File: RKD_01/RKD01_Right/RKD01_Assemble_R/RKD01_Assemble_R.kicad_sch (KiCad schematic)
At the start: 95 parts, among them J2 TRRS, M1 Mark, M2 Mark, M3 Mark, M4 Mark, M5 Mark, M6 Mark, P1 pointing, SW51 SW_Push, SW52 SW_Push, SW53 SW_Push, SW54 SW_Push, SW55 SW_Push, SW56 SW_Push, SW57 SW_Push, SW58 SW_Push, SW59 SW_Push, SW60 SW_Push, SW61 SW_Push, SW62 SW_Push, SW63 SW_Push, SW64 SW_Push, SW65 SW_Push, SW66 SW_Push, SW67 SW_Push, SW68 SW_Push, SW69 SW_Push, SW70 SW_Push, SW71 SW_Push, SW72 SW_Push, SW73 SW_Push, SW74 SW_Push, SW75 SW_Push, SW76 SW_Push, SW77 SW_Push, SW78 SW_Push, SW79 SW_Push, SW80 SW_Push, SW81 SW_Push, SW82 SW_Push, SW83 SW_Push, SW84 SW_Push, SW85 SW_Push, SW86 SW_Push, SW87 SW_Push, SW88 SW_Push, SW89 SW_Push, SW90 SW_Push, SW91 SW_Push, SW92 SW_Push, SW93 SW_Push, U2 ProMicro

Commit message: v1.5
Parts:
- added D75: D, kbd_Parts:Diode_TH_SMD, symbol Device:D
- added M7, M8: Mark, kbd_Hole:m2_Spacer_Hole_hex, symbol BrownSugar_KBD:Mark
- added SW75: SW_Push, kbd_SW:Choc_Hotswap_1u, symbol Switch:SW_Push
- renumbered D75 to D76, D76 to D77, D77 to D78, D78 to D79, D79 to D80, D80 to D81, D81 to D82, D82 to D83, D83 to D84, D84 to D85, D85 to D86, D86 to D87, D87 to D88, D88 to D89, D89 to D90, D90 to D91, D91 to D92, D92 to D94, D93 to D95, SW75 to SW76, SW76 to SW77, SW77 to SW78, SW78 to SW79, SW79 to SW80, SW80 to SW81, SW81 to SW82, SW82 to SW83, SW83 to SW84, SW84 to SW85, SW85 to SW86, SW86 to SW87, SW87 to SW88, SW88 to SW89, SW89 to SW90, SW90 to SW91, SW91 to SW92, SW92 to SW94, SW93 to SW95
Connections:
- net Col4: now also SW75.2
- net Row4: now also D75.1 (K)
- new net: D75.2 (A), SW75.1

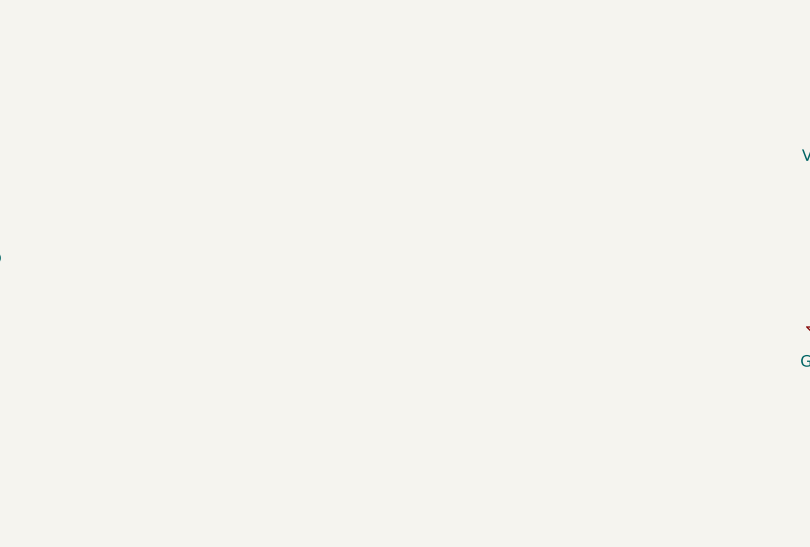
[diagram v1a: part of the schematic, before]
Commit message: OLEDを追加
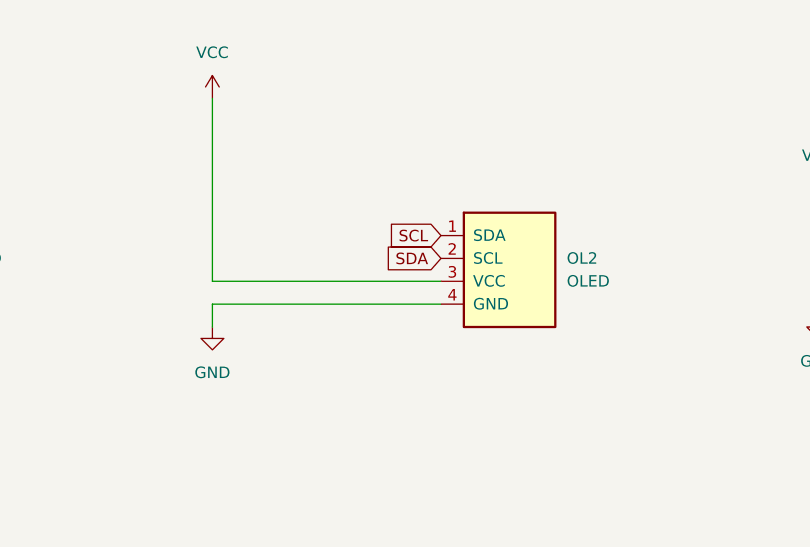
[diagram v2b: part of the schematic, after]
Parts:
- added OL2: OLED, BrownSugar_KBD:OLED_center_module, symbol BrownSugar_KBD:OLED
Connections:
- net GND: now also OL2.4 (GND)
- net SCL: now also OL2.1 (SDA)
- net SDA: now also OL2.2 (SCL)
- net VCC: now also OL2.3 (VCC)

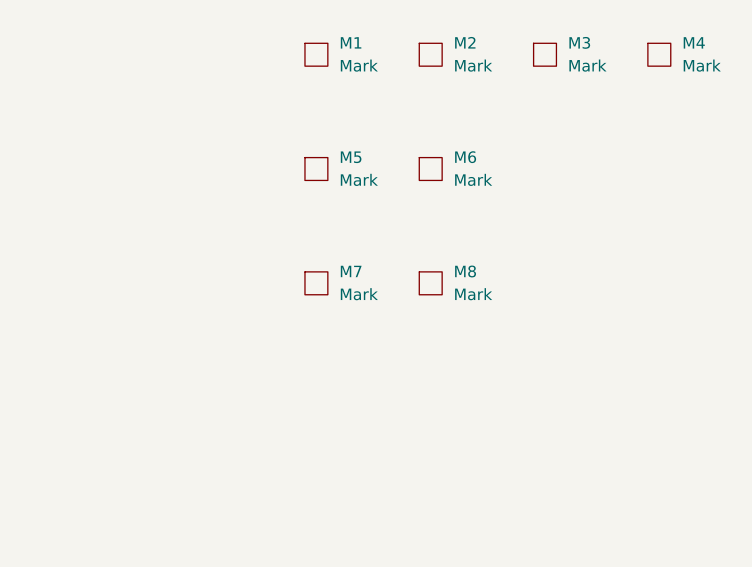
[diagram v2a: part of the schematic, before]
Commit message: スイッチフットプリントをChocV2に修正
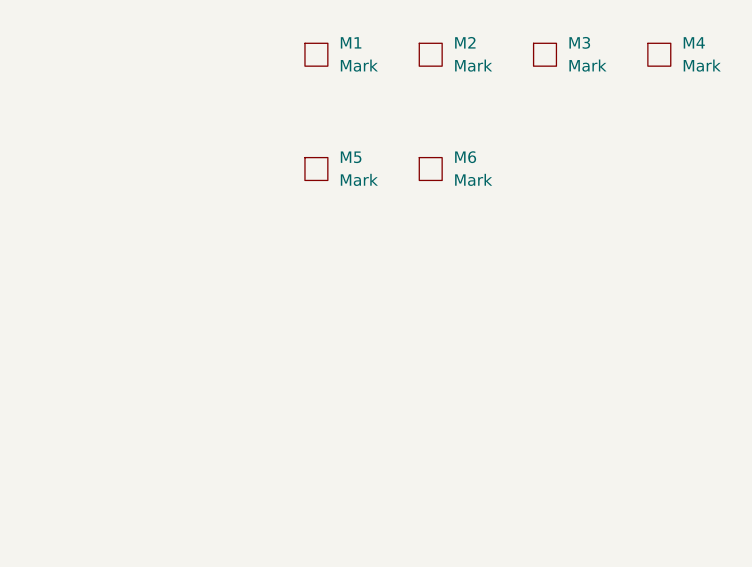
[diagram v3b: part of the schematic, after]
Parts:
- removed M7, M8: Mark, kbd_Hole:m2_Spacer_Hole_hex, symbol BrownSugar_KBD:Mark
- SW51, SW52, SW53, SW54, SW55, SW56, SW57, SW58, SW59, SW60, SW61, SW62, SW63, SW64, SW65, SW66, SW67, SW68, SW69, SW70, SW71, SW72, SW73, SW74, SW75, SW76, SW77, SW78, SW79, SW80, SW81, SW82, SW83, SW84, SW85, SW86, SW87, SW89, SW90, SW92, SW94, SW95: footprint kbd_SW:Choc_Hotswap_1u -> Rikkodo_FootPrint:rkd_Choc_v2_Hotswap_1u
- SW88, SW91: footprint kbd_SW:Choc_Hotswap_2u_Stab -> Rikkodo_FootPrint:rkd_Choc_v2_Hotswap_2u
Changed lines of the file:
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@@
 			)
 		)
-		(property "Footprint" "kbd_SW:Choc_Hotswap_1u"
+		(property "Footprint" "Rikkodo_FootPrint:rkd_Choc_v2_Hotswap_1u"
 			(at 254 198.12 0)
 			(effects
@@
 			)
 		)
-		(property "Footprint" "kbd_SW:Choc_Hotswap_1u"
+		(property "Footprint" "Rikkodo_FootPrint:rkd_Choc_v2_Hotswap_1u"
 			(at 127 198.12 0)
 			(effects
@@
 			)
 		)
-		(property "Footprint" "kbd_SW:Choc_Hotswap_1u"
+		(property "Footprint" "Rikkodo_FootPrint:rkd_Choc_v2_Hotswap_1u"
 			(at 76.2 223.52 0)
 			(effects
@@
 			)
 		)
-		(property "Footprint" "kbd_SW:Choc_Hotswap_1u"
+		(property "Footprint" "Rikkodo_FootPrint:rkd_Choc_v2_Hotswap_1u"
 			(at 101.6 172.72 0)
 			(effects
@@
 			)
 		)
-		(property "Footprint" "kbd_SW:Choc_Hotswap_1u"
+		(property "Footprint" "Rikkodo_FootPrint:rkd_Choc_v2_Hotswap_1u"
 			(at 101.6 147.32 0)
 			(effects
@@
 			)
 		)
-		(property "Footprint" "kbd_SW:Choc_Hotswap_2u_Stab"
+		(property "Footprint" "Rikkodo_FootPrint:rkd_Choc_v2_Hotswap_2u"
 			(at 228.6 172.72 0)
 			(effects
@@
 			)
 		)
-		(property "Footprint" "kbd_SW:Choc_Hotswap_1u"
+		(property "Footprint" "Rikkodo_FootPrint:rkd_Choc_v2_Hotswap_1u"
 			(at 203.2 147.32 0)
 			(effects
@@
 			)
 		)
-		(property "Footprint" "kbd_SW:Choc_Hotswap_1u"
+		(property "Footprint" "Rikkodo_FootPrint:rkd_Choc_v2_Hotswap_1u"
 			(at 203.2 172.72 0)
 			(effects
@@
 			)
 		)
-		(property "Footprint" "kbd_SW:Choc_Hotswap_1u"
+		(property "Footprint" "Rikkodo_FootPrint:rkd_Choc_v2_Hotswap_1u"
 			(at 177.8 172.72 0)
 			(effects
@@
 			)
 		)
-		(property "Footprint" "kbd_SW:Choc_Hotswap_1u"
+		(property "Footprint" "Rikkodo_FootPrint:rkd_Choc_v2_Hotswap_1u"
 			(at 76.2 147.32 0)
 			(effects
@@
 			)
 		)
-		(property "Footprint" "kbd_SW:Choc_Hotswap_1u"
+		(property "Footprint" "Rikkodo_FootPrint:rkd_Choc_v2_Hotswap_1u"
 			(at 50.8 198.12 0)
 			(effects
@@
 			)
 		)
-		(property "Footprint" "kbd_SW:Choc_Hotswap_1u"
+		(property "Footprint" "Rikkodo_FootPrint:rkd_Choc_v2_Hotswap_1u"
 			(at 177.8 223.52 0)
 			(effects
@@
 			)
 		)
-		(property "Footprint" "kbd_SW:Choc_Hotswap_1u"
+		(property "Footprint" "Rikkodo_FootPrint:rkd_Choc_v2_Hotswap_1u"
 			(at 177.8 198.12 0)
 			(effects
@@
 			)
 		)
-		(property "Footprint" "kbd_SW:Choc_Hotswap_1u"
+		(property "Footprint" "Rikkodo_FootPrint:rkd_Choc_v2_Hotswap_1u"
 			(at 228.6 147.32 0)
 			(effects
@@
 	)
 	(symbol
-		(lib_id "BrownSugar_KBD:Mark")
-		(at 304.8 190.5 0)
-		(unit 1)
-		(exclude_from_sim no)
-		(in_bom yes)
-		(on_board yes)
-		(dnp no)
-		(fields_autoplaced yes)
-		(property "Reference" "M7"
-			(at 307.34 189.2299 0)
-			(effects
-				(font
-					(size 1.27 1.27)
-				)
-				(justify left)
-			)
-		)
-		(property "Value" "Mark"
-			(at 307.34 191.7699 0)
-			(effects
-				(font
-					(size 1.27 1.27)
-				)
-				(justify left)
-			)
-		)
-		(property "Footprint" "kbd_Hole:m2_Spacer_Hole_hex"
-			(at 304.8 190.5 0)
-			(effects
-				(font
-					(size 1.27 1.27)
-				)
-				(hide yes)
-			)
-		)
-		(property "Datasheet" ""
-			(at 304.8 190.5 0)
-			(effects
-				(font
-					(size 1.27 1.27)
-				)
-				(hide yes)
-			)
-		)
-		(property "Description" ""
-			(at 304.8 190.5 0)
-			(effects
-				(font
-					(size 1.27 1.27)
-				)
-				(hide yes)
-			)
-		)
-		(instances
-			(project "RKD01_Assemble_R"
-				(path "/19f536aa-aef0-4c4e-9294-f05dcbf6eea3"
-					(reference "M7")
-					(unit 1)
-				)
-			)
-		)
-	)
-	(symbol
 		(lib_id "Switch:SW_Push")
 		(at 127 152.4 0)
@@
 			)
 		)
-		(property "Footprint" "kbd_SW:Choc_Hotswap_1u"
+		(property "Footprint" "Rikkodo_FootPrint:rkd_Choc_v2_Hotswap_1u"
 			(at 127 147.32 0)
 			(effects
@@
 			)
 		)
-		(property "Footprint" "kbd_SW:Choc_Hotswap_1u"
+		(property "Footprint" "Rikkodo_FootPrint:rkd_Choc_v2_Hotswap_1u"
 			(at 254 147.32 0)
 			(effects
@@
 			)
 		)
-		(property "Footprint" "kbd_SW:Choc_Hotswap_1u"
+		(property "Footprint" "Rikkodo_FootPrint:rkd_Choc_v2_Hotswap_1u"
 			(at 177.8 121.92 0)
 			(effects
@@
 			)
 		)
-		(property "Footprint" "kbd_SW:Choc_Hotswap_1u"
+		(property "Footprint" "Rikkodo_FootPrint:rkd_Choc_v2_Hotswap_1u"
 			(at 50.8 223.52 0)
 			(effects
@@
 			)
 		)
-		(property "Footprint" "kbd_SW:Choc_Hotswap_1u"
+		(property "Footprint" "Rikkodo_FootPrint:rkd_Choc_v2_Hotswap_1u"
 			(at 177.8 147.32 0)
 			(effects
@@
 			)
 		)
-		(property "Footprint" "kbd_SW:Choc_Hotswap_1u"
+		(property "Footprint" "Rikkodo_FootPrint:rkd_Choc_v2_Hotswap_1u"
 			(at 101.6 198.12 0)
 			(effects
@@
 			)
 		)
-		(property "Footprint" "kbd_SW:Choc_Hotswap_1u"
+		(property "Footprint" "Rikkodo_FootPrint:rkd_Choc_v2_Hotswap_1u"
 			(at 152.4 147.32 0)
 			(effects
@@
 			)
 		)
-		(property "Footprint" "kbd_SW:Choc_Hotswap_1u"
+		(property "Footprint" "Rikkodo_FootPrint:rkd_Choc_v2_Hotswap_1u"
 			(at 76.2 198.12 0)
 			(effects
@@
 			)
 		)
-		(property "Footprint" "kbd_SW:Choc_Hotswap_1u"
+		(property "Footprint" "Rikkodo_FootPrint:rkd_Choc_v2_Hotswap_1u"
 			(at 228.6 198.12 0)
 			(effects
@@
 			)
 		)
-		(property "Footprint" "kbd_SW:Choc_Hotswap_1u"
+		(property "Footprint" "Rikkodo_FootPrint:rkd_Choc_v2_Hotswap_1u"
 			(at 203.2 223.52 0)
 			(effects
@@
 			)
 		)
-		(property "Footprint" "kbd_SW:Choc_Hotswap_1u"
+		(property "Footprint" "Rikkodo_FootPrint:rkd_Choc_v2_Hotswap_1u"
 			(at 127 223.52 0)
 			(effects
@@
 			)
 		)
-		(property "Footprint" "kbd_SW:Choc_Hotswap_1u"
+		(property "Footprint" "Rikkodo_FootPrint:rkd_Choc_v2_Hotswap_1u"
 			(at 50.8 147.32 0)
 			(effects
@@
 			)
 		)
-		(property "Footprint" "kbd_SW:Choc_Hotswap_1u"
+		(property "Footprint" "Rikkodo_FootPrint:rkd_Choc_v2_Hotswap_1u"
 			(at 76.2 172.72 0)
 			(effects
@@
 			)
 		)
-		(property "Footprint" "kbd_SW:Choc_Hotswap_1u"
+		(property "Footprint" "Rikkodo_FootPrint:rkd_Choc_v2_Hotswap_1u"
 			(at 101.6 223.52 0)
 			(effects
@@
 			)
 		)
-		(property "Footprint" "kbd_SW:Choc_Hotswap_1u"
+		(property "Footprint" "Rikkodo_FootPrint:rkd_Choc_v2_Hotswap_1u"
 			(at 203.2 121.92 0)
 			(effects
@@
 			)
 		)
-		(property "Footprint" "kbd_SW:Choc_Hotswap_1u"
+		(property "Footprint" "Rikkodo_FootPrint:rkd_Choc_v2_Hotswap_1u"
 			(at 254 223.52 0)
 			(effects
@@
 			)
 		)
-		(property "Footprint" "kbd_SW:Choc_Hotswap_1u"
+		(property "Footprint" "Rikkodo_FootPrint:rkd_Choc_v2_Hotswap_1u"
 			(at 203.2 198.12 0)
 			(effects
@@
 			)
 		)
-		(property "Footprint" "kbd_SW:Choc_Hotswap_1u"
+		(property "Footprint" "Rikkodo_FootPrint:rkd_Choc_v2_Hotswap_1u"
 			(at 228.6 223.52 0)
 			(effects
@@
 			)
 		)
-		(property "Footprint" "kbd_SW:Choc_Hotswap_1u"
+		(property "Footprint" "Rikkodo_FootPrint:rkd_Choc_v2_Hotswap_1u"
 			(at 152.4 198.12 0)
 			(effects
@@
 			)
 		)
-		(property "Footprint" "kbd_SW:Choc_Hotswap_2u_Stab"
+		(property "Footprint" "Rikkodo_FootPrint:rkd_Choc_v2_Hotswap_2u"
 			(at 254 121.92 0)
 			(effects
@@
 			)
 		)
-		(property "Footprint" "kbd_SW:Choc_Hotswap_1u"
+		(property "Footprint" "Rikkodo_FootPrint:rkd_Choc_v2_Hotswap_1u"
 			(at 152.4 121.92 0)
 			(effects
@@
 			)
 		)
-		(property "Footprint" "kbd_SW:Choc_Hotswap_1u"
+		(property "Footprint" "Rikkodo_FootPrint:rkd_Choc_v2_Hotswap_1u"
 			(at 101.6 121.92 0)
 			(effects
@@
 			)
 		)
-		(property "Footprint" "kbd_SW:Choc_Hotswap_1u"
+		(property "Footprint" "Rikkodo_FootPrint:rkd_Choc_v2_Hotswap_1u"
 			(at 50.8 121.92 0)
 			(effects
@@
 			)
 		)
-		(property "Footprint" "kbd_SW:Choc_Hotswap_1u"
+		(property "Footprint" "Rikkodo_FootPrint:rkd_Choc_v2_Hotswap_1u"
 			(at 127 172.72 0)
 			(effects
@@
 			)
 		)
-		(property "Footprint" "kbd_SW:Choc_Hotswap_1u"
+		(property "Footprint" "Rikkodo_FootPrint:rkd_Choc_v2_Hotswap_1u"
 			(at 228.6 121.92 0)
 			(effects
@@
 	)
 	(symbol
-		(lib_id "BrownSugar_KBD:Mark")
-		(at 317.5 190.5 0)
-		(unit 1)
-		(exclude_from_sim no)
-		(in_bom yes)
-		(on_board yes)
-		(dnp no)
-		(fields_autoplaced yes)
-		(property "Reference" "M8"
-			(at 320.04 189.2299 0)
-			(effects
-				(font
-					(size 1.27 1.27)
-				)
-				(justify left)
-			)
-		)
-		(property "Value" "Mark"
-			(at 320.04 191.7699 0)
-			(effects
-				(font
-					(size 1.27 1.27)
-				)
-				(justify left)
-			)
-		)
-		(property "Footprint" "kbd_Hole:m2_Spacer_Hole_hex"
-			(at 317.5 190.5 0)
-			(effects
-				(font
-					(size 1.27 1.27)
-				)
-				(hide yes)
-			)
-		)
-		(property "Datasheet" ""
-			(at 317.5 190.5 0)
-			(effects
-				(font
-					(size 1.27 1.27)
-				)
-				(hide yes)
-			)
-		)
-		(property "Description" ""
-			(at 317.5 190.5 0)
-			(effects
-				(font
-					(size 1.27 1.27)
-				)
-				(hide yes)
-			)
-		)
-		(instances
-			(project "RKD01_Assemble_R"
-				(path "/19f536aa-aef0-4c4e-9294-f05dcbf6eea3"
-					(reference "M8")
-					(unit 1)
-				)
-			)
-		)
-	)
-	(symbol
 		(lib_id "Switch:SW_Push")
 		(at 127 127 0)
@@
 			)
 		)
-		(property "Footprint" "kbd_SW:Choc_Hotswap_1u"
+		(property "Footprint" "Rikkodo_FootPrint:rkd_Choc_v2_Hotswap_1u"
 			(at 127 121.92 0)
 			(effects
@@
 			)
 		)
-		(property "Footprint" "kbd_SW:Choc_Hotswap_1u"
+		(property "Footprint" "Rikkodo_FootPrint:rkd_Choc_v2_Hotswap_1u"
 			(at 152.4 172.72 0)
 			(effects
@@
 			)
 		)
-		(property "Footprint" "kbd_SW:Choc_Hotswap_1u"
+		(property "Footprint" "Rikkodo_FootPrint:rkd_Choc_v2_Hotswap_1u"
 			(at 152.4 223.52 0)
 			(effects
@@
 			)
 		)
-		(property "Footprint" "kbd_SW:Choc_Hotswap_1u"
+		(property "Footprint" "Rikkodo_FootPrint:rkd_Choc_v2_Hotswap_1u"
 			(at 50.8 172.72 0)
 			(effects
@@
 			)
 		)
-		(property "Footprint" "kbd_SW:Choc_Hotswap_1u"
+		(property "Footprint" "Rikkodo_FootPrint:rkd_Choc_v2_Hotswap_1u"
 			(at 76.2 121.92 0)
 			(effects
